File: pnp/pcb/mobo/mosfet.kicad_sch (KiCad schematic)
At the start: 5 parts, among them J22 Mosfet, Q1 AO3400A

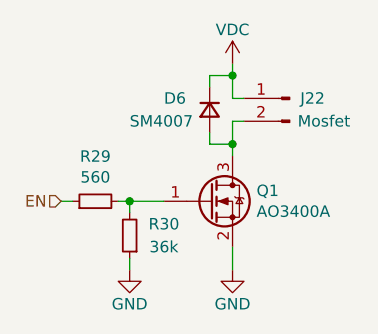
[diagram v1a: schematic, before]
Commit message: another huge chunk of work on rev04 of the mobo. breaks out diag and index pin for TMC2209 sensorless homing. reduces unique part count by consolidating resistor values where possible. replaces full ADC pipeline with monolithic I2C vacuum sensor and an I2C multiplexer due to address collision issues with two sensors. adds solder selectable jumpers for selecting whether an axis uses switch or TMC homing. redoes lots of routing of the SPI lines up to the stepper drivers.
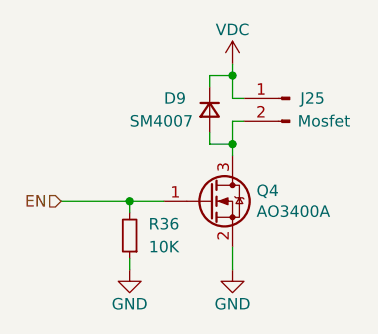
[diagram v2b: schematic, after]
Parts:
- removed R29: 560, Resistor_SMD:R_0805_2012Metric, symbol Device:R_Small
- R36: renamed from R30; value 36k -> 10K
- renumbered D6 to D9, J22 to J25, Q1 to Q4
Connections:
- net EN: now also Q4.1 (G), R36.2
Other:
- company: (none) -> Opulo
- title: Mosfet -> LumenPnP Motherboard
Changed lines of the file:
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@@
   (paper "A4")
   (title_block
-    (title "Mosfet")
+    (title "LumenPnP Motherboard")
     (date "2022-03-29")
     (rev "003")
+    (company "Opulo")
   )
   (junction (at 152.4 91.44) (diameter 0) (color 0 0 0 0)
@@
     (stroke (width 0) (type default) (color 0 0 0 0))
   )
-  (wire (pts (xy 139.7 105.41) (xy 140.97 105.41))
-    (stroke (width 0) (type default) (color 0 0 0 0))
-  )
   (wire (pts (xy 140.97 105.41) (xy 144.78 105.41))
     (stroke (width 0) (type default) (color 0 0 0 0))
@@
     (stroke (width 0) (type default) (color 0 0 0 0))
   )
-  (wire (pts (xy 133.35 105.41) (xy 134.62 105.41))
+  (wire (pts (xy 133.35 105.41) (xy 140.97 105.41))
     (stroke (width 0) (type default) (color 0 0 0 0))
   )
@@
   (symbol (lib_id "Connector:Conn_01x02_Male") (at 158.75 93.98 0) (mirror y)
     (in_bom yes) (on_board yes)
-    (property "Reference" "J22" (id 0) (at 161.29 93.98 0))
+    (property "Reference" "J25" (id 0) (at 161.29 93.98 0))
     (property "Value" "Mosfet" (id 1) (at 162.56 96.52 0))
     (property "Footprint" "Connector_JST:JST_XH_B2B-XH-A_1x02_P2.50mm_Vertical" (id 2) (at 158.75 93.98 0)
@@
   (symbol (lib_id "Transistor_FET:AO3400A") (at 149.86 105.41 0)
     (in_bom yes) (on_board yes)
-    (property "Reference" "Q1" (id 0) (at 155.067 104.2416 0)
+    (property "Reference" "Q4" (id 0) (at 155.067 104.2416 0)
       (effects (font (size 1.27 1.27)) (justify left))
     )
@@
   (symbol (lib_id "power:GND") (at 152.4 113.03 0)
     (in_bom yes) (on_board yes)
-    (property "Reference" "#PWR0188" (id 0) (at 152.4 119.38 0)
+    (property "Reference" "#PWR0194" (id 0) (at 152.4 119.38 0)
       (effects (font (size 1.27 1.27)) hide)
     )
@@
   (symbol (lib_id "Device:R_Small") (at 140.97 109.22 180)
     (in_bom yes) (on_board yes)
-    (property "Reference" "R30" (id 0) (at 144.78 107.95 0))
-    (property "Value" "36k" (id 1) (at 144.78 110.49 0))
+    (property "Reference" "R36" (id 0) (at 144.78 107.95 0))
+    (property "Value" "10K" (id 1) (at 144.78 110.49 0))
     (property "Footprint" "Resistor_SMD:R_0805_2012Metric" (id 2) (at 140.97 109.22 0)
       (effects (font (size 1.27 1.27)) hide)
@@
     (pin "2")
   )
-  (symbol (lib_id "Device:R_Small") (at 137.16 105.41 90)
-    (in_bom yes) (on_board yes)
-    (property "Reference" "R29" (id 0) (at 137.16 100.4316 90))
-    (property "Value" "560" (id 1) (at 137.16 102.743 90))
-    (property "Footprint" "Resistor_SMD:R_0805_2012Metric" (id 2) (at 137.16 105.41 0)
-      (effects (font (size 1.27 1.27)) hide)
-    )
-    (property "Datasheet" "" (id 3) (at 137.16 105.41 0)
-      (effects (font (size 1.27 1.27)) hide)
-    )
-    (property "JLCPCB" "C28636" (id 4) (at 137.16 105.41 0)
-      (effects (font (size 1.27 1.27)) hide)
-    )
-    (property "LCSC" "C28636" (id 5) (at 137.16 105.41 0)
-      (effects (font (size 1.27 1.27)) hide)
-    )
-    (property "Digikey" "RHM560AHCT-ND" (id 6) (at 137.16 105.41 0)
-      (effects (font (size 1.27 1.27)) hide)
-    )
-    (property "Mouser" "667-ERJ-6ENF5600V" (id 7) (at 137.16 105.41 0)
-      (effects (font (size 1.27 1.27)) hide)
-    )
-    (pin "1")
-    (pin "2")
-  )
   (symbol (lib_id "Device:D_Small") (at 149.86 95.25 270)
     (in_bom yes) (on_board yes)
-    (property "Reference" "D6" (id 0) (at 144.78 93.98 90)
+    (property "Reference" "D9" (id 0) (at 144.78 93.98 90)
       (effects (font (size 1.27 1.27)) (justify left))
     )
@@
   (symbol (lib_id "power:VDC") (at 152.4 90.17 0)
     (in_bom yes) (on_board yes)
-    (property "Reference" "#PWR0187" (id 0) (at 152.4 92.71 0)
+    (property "Reference" "#PWR0193" (id 0) (at 152.4 92.71 0)
       (effects (font (size 1.27 1.27)) hide)
     )
@@
   (symbol (lib_id "power:GND") (at 140.97 113.03 0)
     (in_bom yes) (on_board yes)
-    (property "Reference" "#PWR0106" (id 0) (at 140.97 119.38 0)
-      (effects (font (size 1.27 1.27)) hide)
-    )
+    (property "Reference" "#PWR0104" (id 0) (at 140.97 119.38 0)
+      (effects (font (size 1.27 1.27)) hide)
+    )

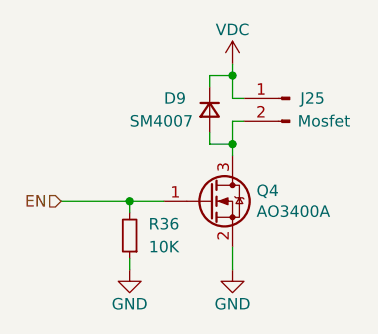
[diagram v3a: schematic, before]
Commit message: fixes erc errors about pin connectivity
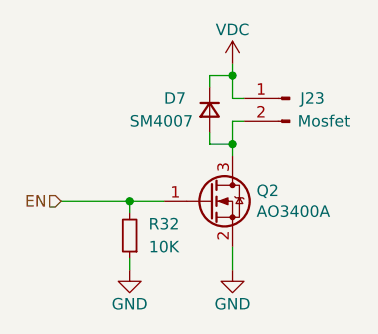
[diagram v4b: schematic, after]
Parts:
- renumbered D9 to D7, J25 to J23, Q4 to Q2, R36 to R32
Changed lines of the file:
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@@
-    (stroke (width 0) (type default) (color 0 0 0 0))
-  )
-  (wire (pts (xy 152.4 110.49) (xy 152.4 113.03))
     (stroke (width 0) (type default) (color 0 0 0 0))
   )
@@
   )
   (wire (pts (xy 152.4 93.98) (xy 152.4 91.44))
+    (stroke (width 0) (type default) (color 0 0 0 0))
+  )
+  (wire (pts (xy 152.4 110.49) (xy 152.4 113.03))
     (stroke (width 0) (type default) (color 0 0 0 0))
   )
@@
   (symbol (lib_id "Connector:Conn_01x02_Male") (at 158.75 93.98 0) (mirror y)
     (in_bom yes) (on_board yes)
-    (property "Reference" "J25" (id 0) (at 161.29 93.98 0))
+    (property "Reference" "J23" (id 0) (at 161.29 93.98 0))
     (property "Value" "Mosfet" (id 1) (at 162.56 96.52 0))
     (property "Footprint" "Connector_JST:JST_XH_B2B-XH-A_1x02_P2.50mm_Vertical" (id 2) (at 158.75 93.98 0)
@@
   (symbol (lib_id "Transistor_FET:AO3400A") (at 149.86 105.41 0)
     (in_bom yes) (on_board yes)
-    (property "Reference" "Q4" (id 0) (at 155.067 104.2416 0)
+    (property "Reference" "Q2" (id 0) (at 155.067 104.2416 0)
       (effects (font (size 1.27 1.27)) (justify left))
     )
@@
     (pin "3")
   )
-  (symbol (lib_id "power:GND") (at 152.4 113.03 0)
+  (symbol (lib_id "power:GND") (at 152.4 113.03 0) (mirror y)
     (in_bom yes) (on_board yes)
     (property "Reference" "#PWR0188" (id 0) (at 152.4 119.38 0)
@@
   (symbol (lib_id "Device:R_Small") (at 140.97 109.22 180)
     (in_bom yes) (on_board yes)
-    (property "Reference" "R36" (id 0) (at 144.78 107.95 0))
+    (property "Reference" "R32" (id 0) (at 144.78 107.95 0))
     (property "Value" "10K" (id 1) (at 144.78 110.49 0))
     (property "Footprint" "Resistor_SMD:R_0805_2012Metric" (id 2) (at 140.97 109.22 0)
@@
   (symbol (lib_id "Device:D_Small") (at 149.86 95.25 270)
     (in_bom yes) (on_board yes)
-    (property "Reference" "D9" (id 0) (at 144.78 93.98 90)
+    (property "Reference" "D7" (id 0) (at 144.78 93.98 90)
       (effects (font (size 1.27 1.27)) (justify left))
     )
